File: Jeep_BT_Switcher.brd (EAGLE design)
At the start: 43.9 x 36.6 mm, 26 parts, among them J1 MF-CON-2.54mm-01x06, J2 MF-CON-2.54mm-01x04, U1 AZ4558C, U2 MAX4544CSA+, U3 MAX4544CSA+

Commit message: Added EXT power connector.
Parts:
- added J3: MF-CON-2.54mm-01x02, MF_Connectors:PTH_2.54MM_01X02
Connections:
- net GND: now also J3.P$2
- net VCC: now also J3.P$1
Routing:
- net VCC: track 140.1 -> 147.0 mm
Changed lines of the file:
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@@
 <attribute name="NAME" x="13.44" y="16.34" size="1.016" layer="25" font="vector" ratio="16"/>
+</element>
+<element name="J3" library="MF_Connectors" package="PTH_2.54MM_01X02" value="MF-CON-2.54mm-01x02" x="30.988" y="34.798" smashed="yes">
+<attribute name="LABEL02" value="GND" x="32.258" y="33.528" size="1.016" layer="22" font="vector" ratio="16" rot="R90" align="center-right"/>
+<attribute name="HOUSEPART" value="YES" x="30.988" y="34.798" size="1.778" layer="27" display="off"/>
+<attribute name="LABEL01" value="VCC" x="29.718" y="33.528" size="1.016" layer="22" font="vector" ratio="16" rot="R90" align="center-right"/>
+<attribute name="MPN" value="MF-CON-2.54mm-01x02" x="30.988" y="34.798" size="1.778" layer="27" display="off"/>
+<attribute name="POPULATE" value="1" x="30.988" y="34.798" size="1.778" layer="27" display="off"/>
+<attribute name="URL" value="https://factory.macrofab.com/part/MF-CON-2.54mm-01x02" x="30.988" y="34.798" size="1.778" layer="27" display="off"/>
+<attribute name="NAME" x="26.436" y="34.52" size="1.016" layer="25" font="vector" ratio="16"/>
 </element>
 </elements>
@@
 <wire x1="41.148" y1="24.892" x2="36.83" y2="24.892" width="0.6096" layer="1"/>
 <wire x1="36.83" y1="24.892" x2="33.782" y2="27.94" width="0.6096" layer="1"/>
-<wire x1="33.782" y1="27.94" x2="29.21" y2="27.94" width="0.6096" layer="1"/>
+<wire x1="33.782" y1="27.94" x2="31.242" y2="27.94" width="0.6096" layer="1"/>
+<wire x1="29.718" y1="27.94" x2="29.21" y2="27.94" width="0.6096" layer="1"/>
 <wire x1="29.21" y1="27.94" x2="28.067" y2="26.797" width="0.6096" layer="1"/>
 <wire x1="28.067" y1="26.797" x2="28.067" y2="24.544" width="0.6096" layer="1"/>
@@
 <wire x1="16.19" y1="18.288" x2="16.256" y2="18.288" width="0.3048" layer="1"/>
 <wire x1="16.256" y1="18.288" x2="16.256" y2="17.272" width="0.3048" layer="1"/>
+<contactref element="J3" pad="P$1"/>
+<wire x1="29.718" y1="34.798" x2="29.718" y2="27.94" width="0.6096" layer="1"/>
+<wire x1="29.718" y1="27.94" x2="31.242" y2="27.94" width="0.6096" layer="1"/>
 </signal>
 <signal name="GND">
@@
 <via x="12.954" y="18.288" extent="1-16" drill="0.6"/>
 <wire x1="12.954" y1="18.288" x2="12.954" y2="18.542" width="0.3048" layer="16"/>
+<contactref element="J3" pad="P$2"/>
 </signal>
 <signal name="N$1">

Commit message: Added cam files and XYRS
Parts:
- added U$11: LHE_FRAME, PP_Aesthetics:LHE_FRAME
- added U$12: MF_LOGOLOGO_SMALL, PP_Aesthetics:MF_LOGO_SMALL
- added U$13: LHE_LOGOLHE_LOGO, PP_Aesthetics:LHE_LOGO
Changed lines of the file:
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@@
 <?xml version="1.0" encoding="utf-8"?>
 <!DOCTYPE eagle SYSTEM "eagle.dtd">
-<eagle version="7.6.0">
+<eagle version="7.4.0">
 <drawing>
 <settings>
@@
 <layer number="106" name="bPlate" color="7" fill="1" visible="no" active="yes"/>
 <layer number="107" name="Crop" color="7" fill="1" visible="no" active="yes"/>
+<layer number="108" name="centerline" color="7" fill="1" visible="yes" active="yes"/>
 <layer number="116" name="Patch_BOT" color="9" fill="4" visible="no" active="yes"/>
 <layer number="121" name="_tsilk" color="7" fill="1" visible="no" active="yes"/>
 <layer number="122" name="_bsilk" color="7" fill="1" visible="no" active="yes"/>
 <layer number="125" name="_tNames" color="7" fill="1" visible="no" active="yes"/>
+<layer number="128" name="128bmp" color="1" fill="10" visible="yes" active="yes"/>
+<layer number="129" name="129bmp" color="2" fill="4" visible="yes" active="yes"/>
+<layer number="130" name="130bmp" color="2" fill="1" visible="yes" active="yes"/>
+<layer number="131" name="prix" color="7" fill="1" visible="yes" active="yes"/>
+<layer number="132" name="test" color="7" fill="1" visible="yes" active="yes"/>
 <layer number="144" name="Drill_legend" color="7" fill="1" visible="no" active="yes"/>
 <layer number="151" name="HeatSink" color="7" fill="1" visible="no" active="yes"/>
@@
 <attribute name="POPULATE" value="1" x="30.988" y="34.798" size="1.778" layer="27" display="off"/>
 <attribute name="URL" value="https://factory.macrofab.com/part/MF-CON-2.54mm-01x02" x="30.988" y="34.798" size="1.778" layer="27" display="off"/>
-<attribute name="NAME" x="26.436" y="34.52" size="1.016" layer="25" font="vector" ratio="16"/>
-</element>
+<attribute name="NAME" x="30.246" y="32.234" size="1.016" layer="25" font="vector" ratio="16"/>
+</element>
+<element name="U$11" library="PP_Aesthetics" package="LHE_FRAME" value="LHE_FRAME" x="9.398" y="30.226">
+<attribute name="REVNUM" value="REV: 2" x="9.398" y="30.226" size="1.778" layer="27" display="off"/>
+<attribute name="DNAME" value="Parker Dillmann" x="9.398" y="30.226" size="1.778" layer="27" display="off"/>
+</element>
+<element name="U$12" library="PP_Aesthetics" package="MF_LOGO_SMALL" value="MF_LOGOLOGO_SMALL" x="37.338" y="22.606"/>
+<element name="U$13" library="PP_Aesthetics" package="LHE_LOGO" value="LHE_LOGOLHE_LOGO" x="22.352" y="30.226" rot="MR0"/>
 </elements>
 <signals>

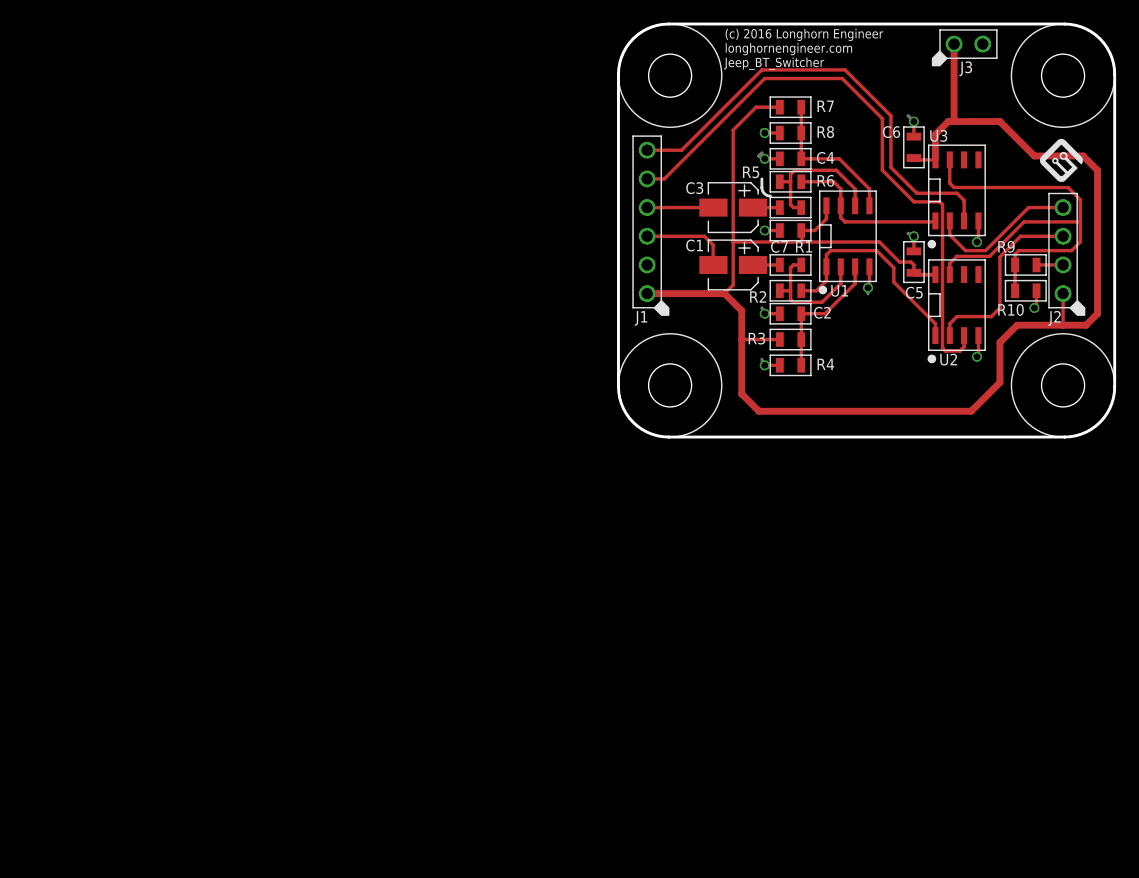
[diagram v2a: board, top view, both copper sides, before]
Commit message: Adding built in BT module.
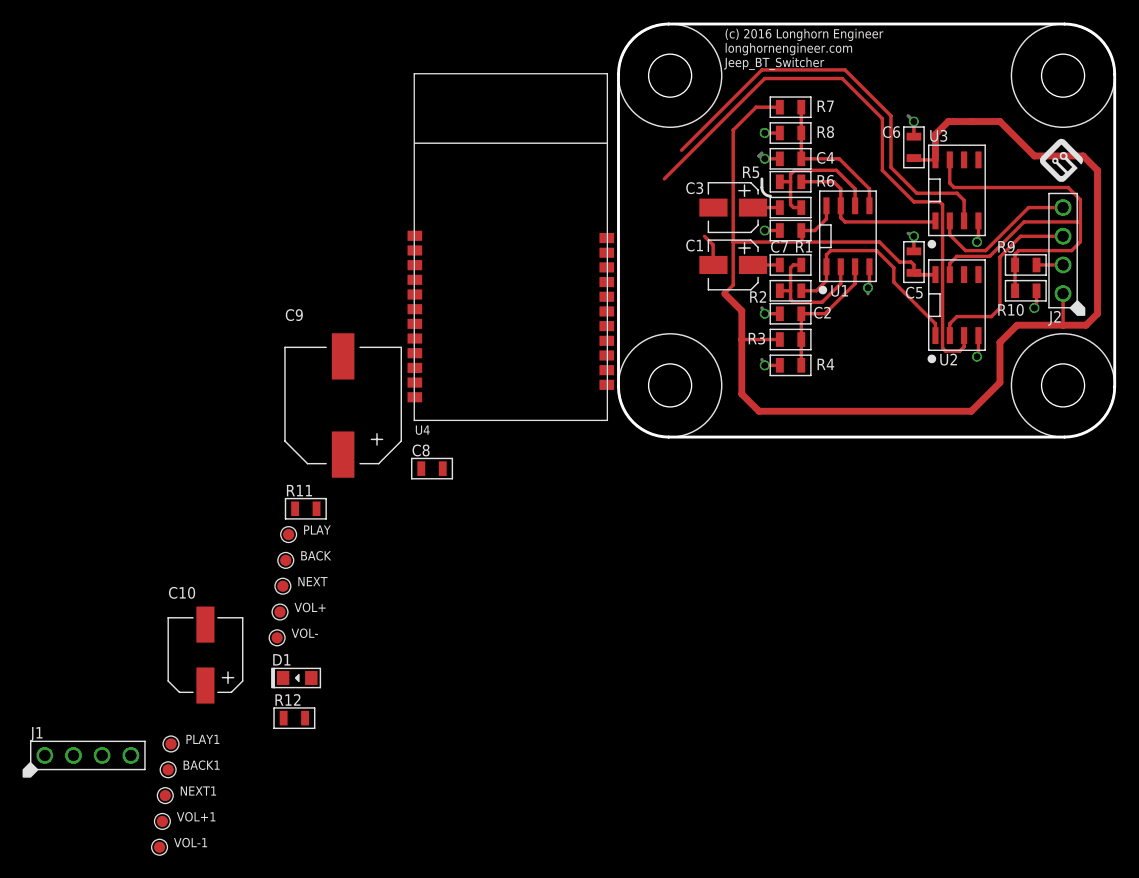
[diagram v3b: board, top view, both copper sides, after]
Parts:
- removed J3: MF-CON-2.54mm-01x02, MF_Connectors:PTH_2.54MM_01X02
- added BACK, BACK1, NEXT, NEXT1, PLAY, PLAY1, VOL+, VOL+1, VOL-, VOL-1: (no value), PP_Connectors:ROUND_TP
- added C10: 47uF, MF_Passives:CP6.3MM
- added C8: 0.1uF, MF_Passives:C0805
- added C9: 220uF, MF_Passives:CP10MM
- added D1: MF-LED-0805-RED, MF_LEDs:LED0805
- added R11: 10K, MF_Passives:R0805
- added R12: 470, MF_Passives:R0805
- added U4: XS-3868, PP_Sensors:XS3868
- J1: value MF-CON-2.54mm-01x06 -> MF-CON-2.54mm-01x04; device MF_Connectors:PTH_2.54MM_01X06 -> MF_Connectors:PTH_2.54MM_01X04
- moved J1 68.4 mm to (-47.0, -28.2), turned to 0 degrees
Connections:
- new net 1.8V: BACK1.P$1, C9.P$1, NEXT1.P$1, PLAY1.P$1, R11.P$2, U4.1.8V_OUT, VOL+1.P$1, VOL-1.P$1
- new net 4.0V: C10.P$1, R12.P$1, U4.VBAT
- new net BACK: BACK.P$1, U4.BACK
- new net LED: D1.CATHODE, U4.CH.STAT.
- new net N$10: D1.ANODE, R12.P$2
- new net N$8: U4.AGND
- new net NEXT: NEXT.P$1, U4.NEXT
- new net PLAY: PLAY.P$1, U4.PLAY
- new net RST: C8.P$1, R11.P$1, U4.RST
- new net VOL+: U4.VOL+, VOL+.P$1
- new net VOL-: U4.VOL-, VOL-.P$1
- net BT_L: now also U4.ALEFT; no longer J1.P$3
- net BT_R: now also U4.ARIGHT; no longer J1.P$4
- net GND: now also C10.P$2, C8.P$2, C9.P$2, U4.GND; no longer J3.P$2
- net JEEP_IN_L: now also J1.P$3; no longer J1.P$5
- net JEEP_IN_R: now also J1.P$4; no longer J1.P$6
- net VCC: no longer J3.P$1
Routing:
- net VCC: track 147.0 -> 133.2 mm
- net BT_R: track 5.87 -> 0.00 mm
- net BT_L: track 7.95 -> 2.87 mm
- net JEEP_IN_R: track 40.3 -> 37.2 mm
- net JEEP_IN_L: track 53.0 -> 51.5 mm
